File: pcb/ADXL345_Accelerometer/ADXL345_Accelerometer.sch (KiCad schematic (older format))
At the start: 16 parts, among them J1 Conn_01x09, Q1 BSS138, Q2 BSS138, U1 ADXL345_Library, U2 AP2112K-3.3

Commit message: Correcciones
Se corrigieron segun las recomendaciones realizadas por el docente.
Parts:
- U1: value ADXL345_Library -> ADXL345
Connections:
- net +3V3: now also R2.2, U1.1 (VDDI/O); no longer R2.1, U1.3 (RES)
- net GND: now also U1.2 (GND); no longer U1.1 (VDDI/O)
- net SCL: now also Q2.2 (S), R5.1; no longer Q2.3 (D), R5.2
- net VIN: now also R5.2; no longer R5.1
- net SDO: now reaches U1.12 (SDO)
- net SDO: now also J1.7 (Pin_7), R6.1
- net at U1.13 (SDA/SDI): now also Q1.2 (S), R1.2
- removed net SCL_3V: Q2.2 (S), R2.2, U1.14 (SCL/SCK)
- net SDA\SDIO renamed SDA
- removed net SDA\SDIO_3V: Q1.2 (S), R1.2, U1.10 (NC)
- removed net SDO\ADDR: J1.7 (Pin_7), R6.1, U1.11 (RES)
- new net: Q2.3 (D), R2.1, U1.14 (SCL/SCK)
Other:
- moved on the sheet: C1, C2, D1, H1, H2, J1, Q1, Q2, R1, R2, R3, R4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

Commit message: Correcciones
Se corrigieron detalles y se agregaron códigos de catálogo recomendados.
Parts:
- J1: Digi-Key (none) -> 10129378-909003BLF-ND; Link (none) -> https://ar.mouser.com/ProductDetail/Amphenol-FCI/10129378-9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; Manufacturer (none) -> Amphenol FCI; Supplier (none) -> Mouser
- Q1, Q2: Digi-Key (none) -> BSS138CT-ND; Link (none) -> https://www.digikey.com/product-detail/en/on-semiconductor/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; Manufacturer (none) -> Semiconductor Components Industries, LLC; Supplier (none) -> Digikey
- U1: Digi-Key (none) -> ADXL345BCCZ-ND; Link (none) -> https://www.digikey.com/product-detail/en/analog-devices-in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; Manufacturer (none) -> Analog Devices, Inc.; Supplier (none) -> Digikey
- U2: Digi-Key (none) -> AP2112K-3.3TRG1DITR-ND; Link (none) -> https://www.digikey.com/product-detail/en/diodes-incorporat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; Manufacturer (none) -> Diodes Incorporated; Supplier (none) -> Digikey
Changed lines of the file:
@@
 F 1 "ADXL345" V 6053 4224 50  0000 C CNN
 F 2 "Package_LGA:LGA-14_3x5mm_P0.8mm_LayoutBorder1x6y" H 6200 4125 50  0001 C CNN
-F 3 "" H 6200 4125 50  0001 C CNN
+F 3 "https://www.analog.com/media/en/technical-documentation/data-sheets/ADXL345.pdf" H 6200 4125 50  0001 C CNN
+F 4 "Analog Devices, Inc." V 6200 3550 50  0001 C CNN "Manufacturer"
+F 5 "https://ar.mouser.com/ProductDetail/Analog-Devices/ADXL345BCCZ?qs=WIvQP4zGanhoa7YOkGtvEg%3D%3D" V 6200 3550 50  0001 C CNN "Link"
+F 6 "Mouser" V 6200 3550 50  0001 C CNN "Supplier"
+F 7 "https://www.digikey.com/product-detail/en/analog-devices-inc/ADXL345BCCZ/ADXL345BCCZ-ND/2034829" V 6200 3550 50  0001 C CNN "Link"
+F 8 "Digikey" V 6200 3550 50  0001 C CNN "Supplier"
+F 9 "ADXL345BCCZ-ND" V 6200 3550 50  0001 C CNN "Digi-Key"
 	1    6200 3550
 	0    1    1    0
@@
 F 2 "Package_TO_SOT_SMD:SOT-23-5" H 5300 1975 50  0001 C CNN
 F 3 "https://www.diodes.com/assets/Datasheets/AP2112.pdf" H 5300 1750 50  0001 C CNN
+F 4 "Diodes Incorporated" H 5300 1650 50  0001 C CNN "Manufacturer"
+F 5 "https://ar.mouser.com/ProductDetail/Diodes-Incorporated/AP2112K-33TRG1?qs=x6A8l6qLYDDPYHosCdzh%2FA%3D%3D" H 5300 1650 50  0001 C CNN "Link"
+F 6 "Mouser" H 5300 1650 50  0001 C CNN "Supplier"
+F 7 "https://www.digikey.com/product-detail/en/diodes-incorporated/AP2112K-3-3TRG1/AP2112K-3-3TRG1DITR-ND/4470746" H 5300 1650 50  0001 C CNN "Link"
+F 8 "Digikey" H 5300 1650 50  0001 C CNN "Supplier"
+F 9 "AP2112K-3.3TRG1DITR-ND" H 5300 1650 50  0001 C CNN "Digi-Key"
 	1    5300 1650
 	1    0    0    -1
@@
 F 1 "Conn_01x09" V 3800 3300 50  0000 L CNN
 F 2 "Connector_PinHeader_2.54mm:PinHeader_1x09_P2.54mm_Vertical" H 3650 3650 50  0001 C CNN
-F 3 "~" H 3650 3650 50  0001 C CNN
+F 3 "https://www.amphenol-icc.com/media/wysiwyg/files/documentation/datasheet/boardwiretoboard/bwb_bergstik.pdf" H 3650 3650 50  0001 C CNN
+F 4 "Amphenol FCI" V 3650 3650 50  0001 C CNN "Manufacturer"
+F 5 "https://ar.mouser.com/ProductDetail/Amphenol-FCI/10129378-909003BLF?qs=0lQeLiL1qyYKryXpJ%252BfC%252BQ%3D%3D" V 3650 3650 50  0001 C CNN "Link"
+F 6 "Mouser" V 3650 3650 50  0001 C CNN "Supplier"
+F 7 "10129378-909003BLF-ND" V 3650 3650 50  0001 C CNN "Digi-Key"
 	1    3650 3650
 	-1   0    0    -1
@@
 F 1 "BSS138" V 5700 5800 50  0000 C CNN
 F 2 "Package_TO_SOT_SMD:SOT-23" H 5550 5725 50  0001 L CIN
-F 3 "https://www.fairchildsemi.com/datasheets/BS/BSS138.pdf" H 5350 5800 50  0001 L CNN
+F 3 "https://www.onsemi.com/pub/Collateral/BSS138-D.PDF" H 5350 5800 50  0001 L CNN
+F 4 "Semiconductor Components Industries, LLC " V 5350 5800 50  0001 C CNN "Manufacturer"
+F 5 "https://ar.mouser.com/ProductDetail/ON-Semiconductor-Fairchild/BSS138?qs=HK%252BeIG1iaahCeqBvjB4arg%3D%3D" V 5350 5800 50  0001 C CNN "Link"
+F 6 "Mouser" V 5350 5800 50  0001 C CNN "Supplier"
+F 7 "https://www.digikey.com/product-detail/en/on-semiconductor/BSS138/BSS138CT-ND/244294" V 5350 5800 50  0001 C CNN "Link"
+F 8 "Digikey" V 5350 5800 50  0001 C CNN "Supplier"
+F 9 "BSS138CT-ND" V 5350 5800 50  0001 C CNN "Digi-Key"
 	1    5350 5800
 	0    1    1    0
@@
 F 1 "BSS138" V 6000 4900 50  0000 C CNN
 F 2 "Package_TO_SOT_SMD:SOT-23" H 5950 4825 50  0001 L CIN
-F 3 "https://www.fairchildsemi.com/datasheets/BS/BSS138.pdf" H 5750 4900 50  0001 L CNN
+F 3 "https://www.onsemi.com/pub/Collateral/BSS138-D.PDF" H 5750 4900 50  0001 L CNN
+F 4 "Semiconductor Components Industries, LLC " V 5750 4900 50  0001 C CNN "Manufacturer"
+F 5 "https://ar.mouser.com/ProductDetail/ON-Semiconductor-Fairchild/BSS138?qs=HK%252BeIG1iaahCeqBvjB4arg%3D%3D" V 5750 4900 50  0001 C CNN "Link"
+F 6 "Mouser" V 5750 4900 50  0001 C CNN "Supplier"
+F 7 "https://www.digikey.com/product-detail/en/on-semiconductor/BSS138/BSS138CT-ND/244294" V 5750 4900 50  0001 C CNN "Link"
+F 8 "Digikey" V 5750 4900 50  0001 C CNN "Supplier"
+F 9 " BSS138CT-ND" V 5750 4900 50  0001 C CNN "Digi-Key"
 	1    5750 4900
 	0    -1   -1   0

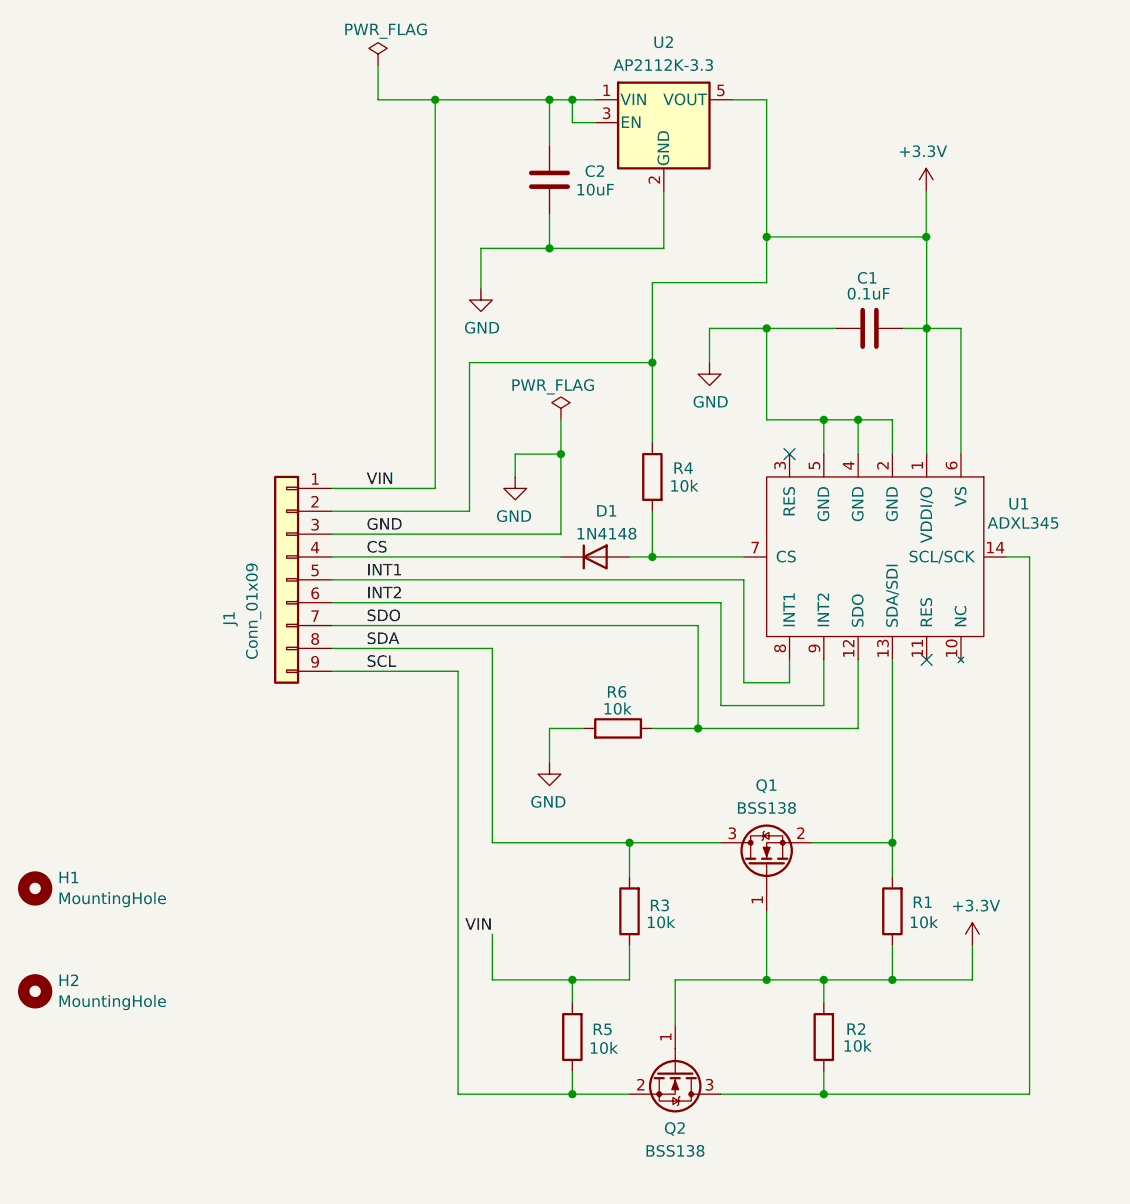
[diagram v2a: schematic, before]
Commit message: Se agregaron fiduciales
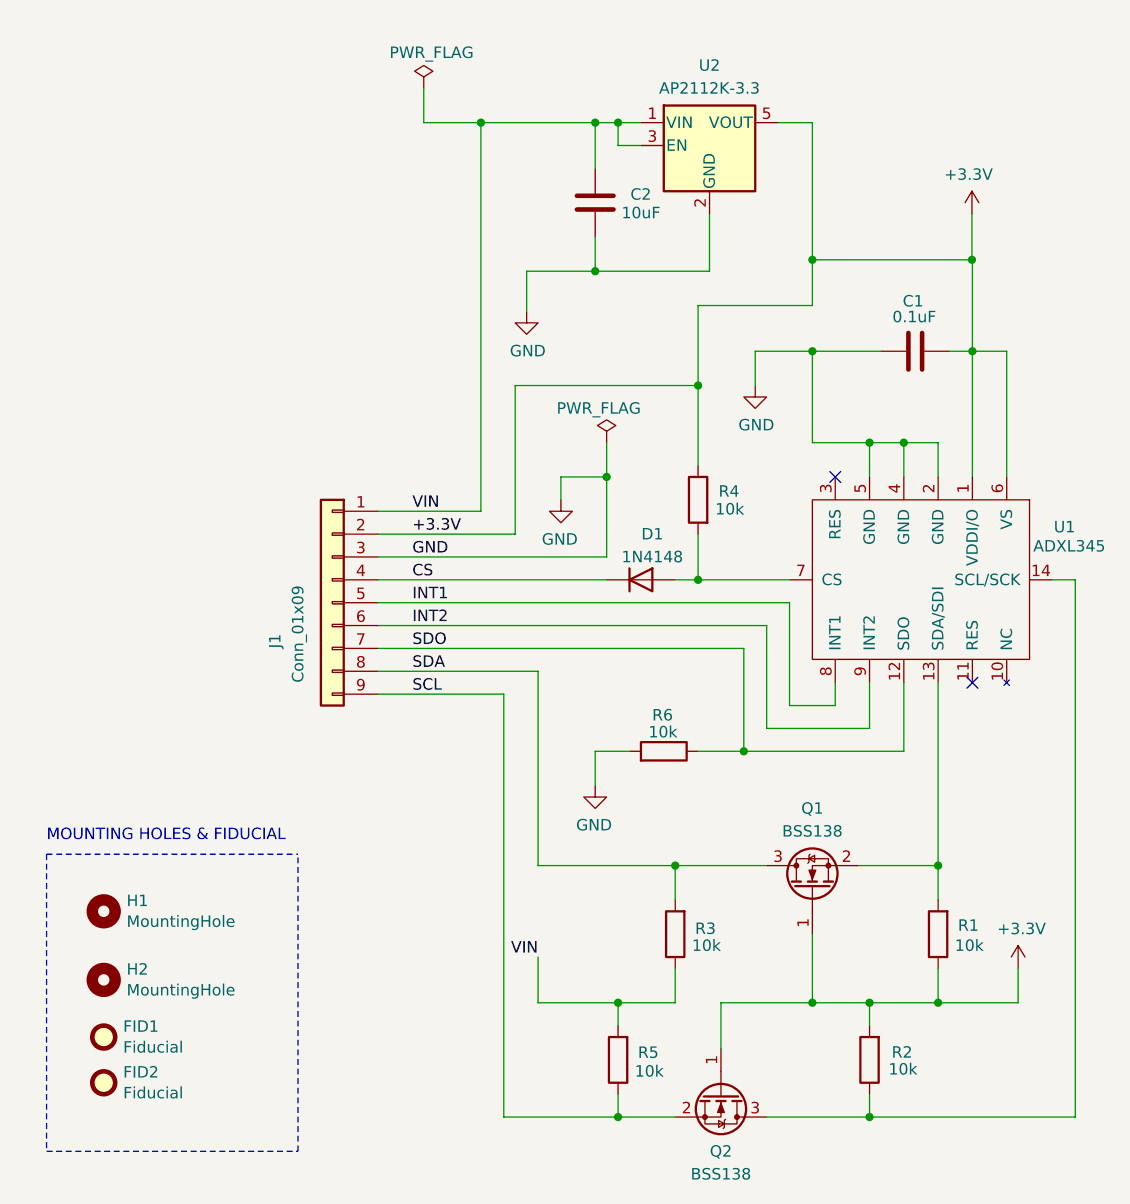
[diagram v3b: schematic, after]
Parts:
- added FID1, FID2: Fiducial, Fiducial:Fiducial_0.5mm_Mask1.5mm, symbol Mechanical:Fiducial
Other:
- note added: "MOUNTING HOLES & FIDUCIAL"
- moved on the sheet: C1, C2, D1, H1, H2, J1, Q1, Q2, R1, R2, R3, R4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

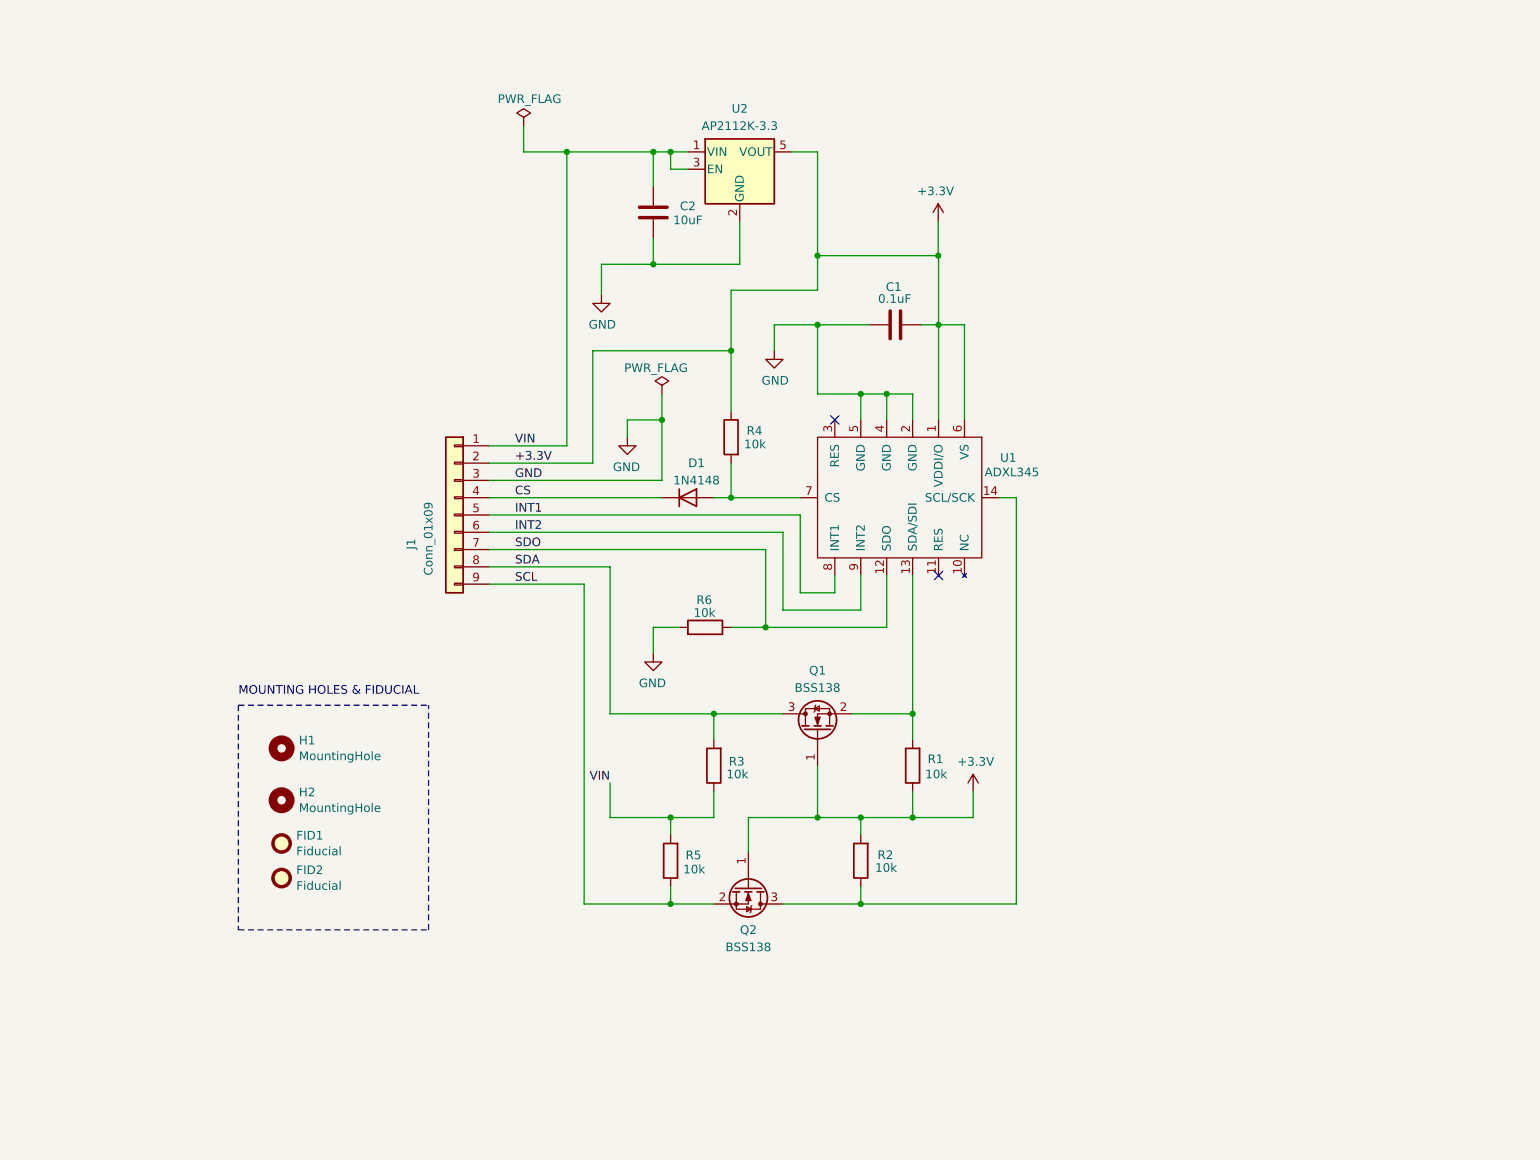
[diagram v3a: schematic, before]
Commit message: Correcciones
Se hicieron las correcciones de acuerdo a las recomendaciones del docente.
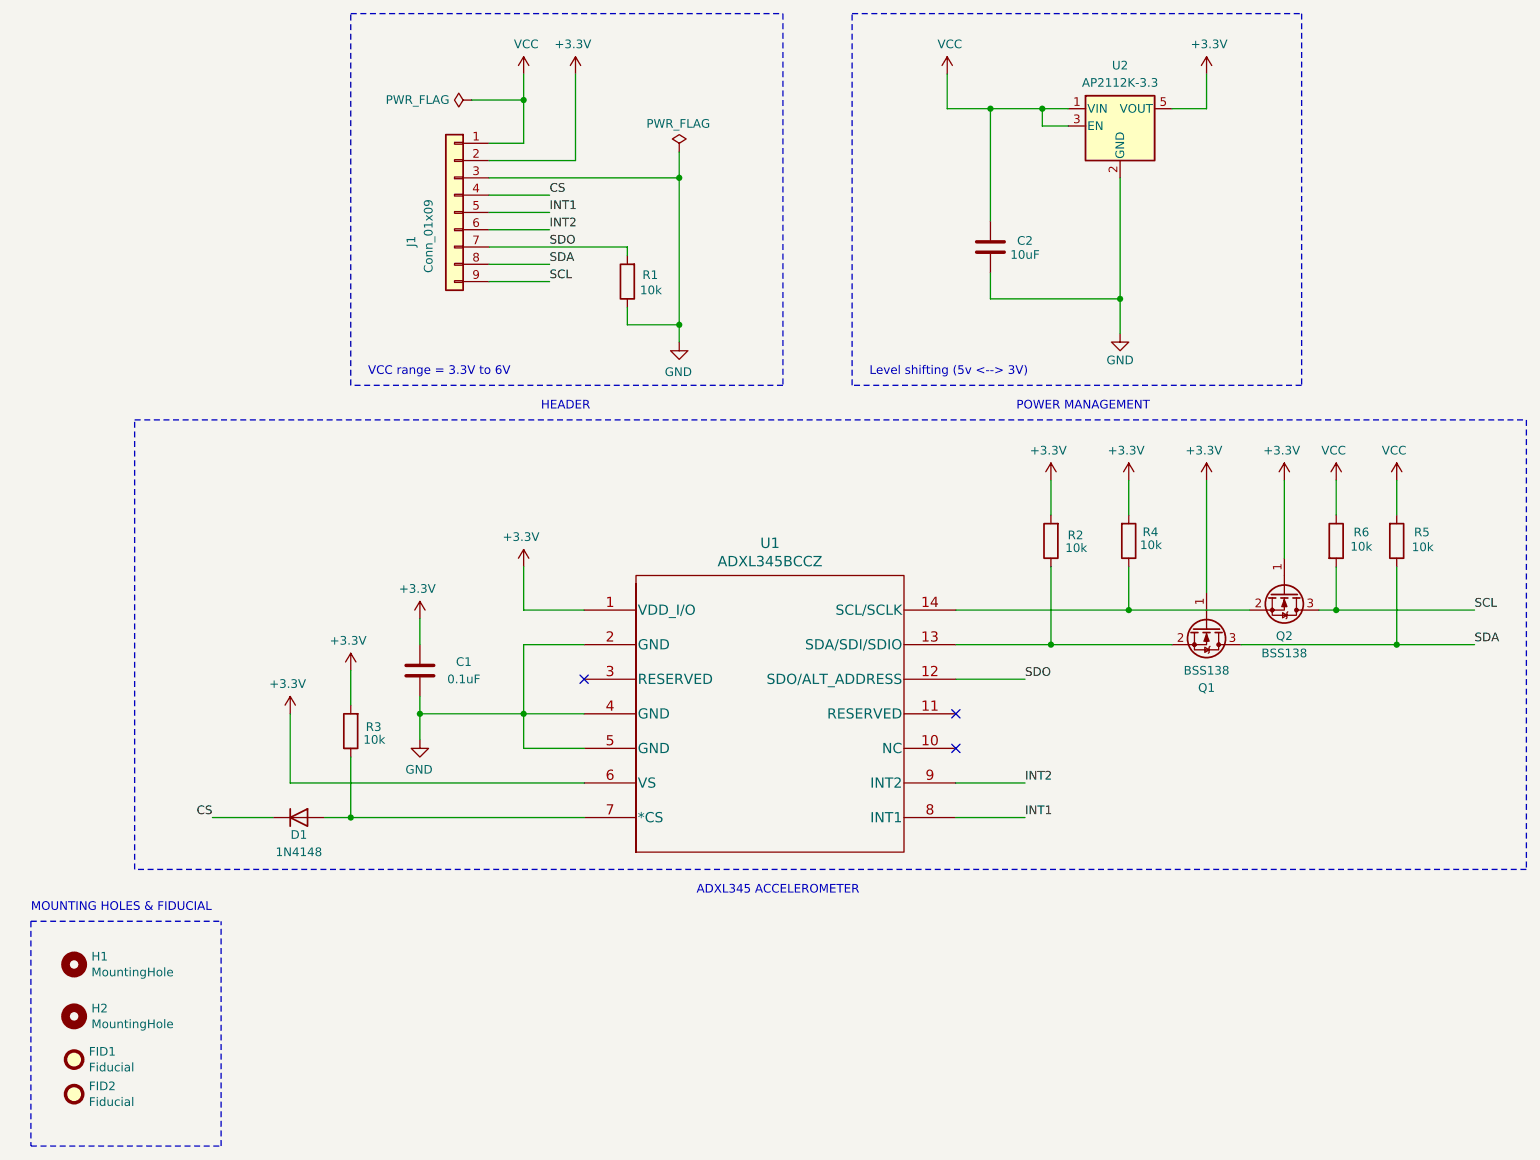
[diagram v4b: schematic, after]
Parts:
- removed U1: ADXL345, Package_LGA:LGA-14_3x5mm_P0.8mm_LayoutBorder1x6y, symbol ADXL345:ADXL345_Library
- added U1: ADXL345BCCZ, Package_LGA:LGA-14_3x5mm_P0.8mm_LayoutBorder1x6y, symbol ADXL345BCCZ:ADXL345BCCZ
- R1, R2, R3, R4, R5, R6: footprint Resistor_SMD:R_0603_1608Metric -> Diode_SMD:D_0805_2012Metric
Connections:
- net +3V3: now also C1.2, R3.2, R4.2, U1.1 (VDD_I/O), U1.6 (VS); no longer C1.1, R1.1, R4.1
- net GND: now also C1.1, R1.1, U1.2 (GND), U1.4 (GND), U1.5 (GND); no longer C1.2, R6.2
- net INT1: now also U1.8 (INT1)
- net INT2: now also U1.9 (INT2)
- net SCL: now also Q2.3 (D), R6.2; no longer Q2.2 (S), R5.1
- net SDA: now also R5.1; no longer R3.2
- net SDO: now also R1.2, U1.12 (SDO/ALT_ADDRESS); no longer R6.1
- net at D1.2 (A): now also R3.1, U1.7 (*CS); no longer R4.2
- net at Q1.2 (S): now also R2.1, U1.13 (SDA/SDI/SDIO); no longer R1.2
- net VIN renamed VCC
- net VCC: now also R6.1; no longer R3.1
- new net: Q2.2 (S), R4.1, U1.14 (SCL/SCLK)
- no-connect marks 2 -> 3
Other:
- note added: "ADXL345 ACCELEROMETER"
- note added: "HEADER"
- note added: "Level shifting (5v <--> 3V)"
- note added: "POWER MANAGEMENT"
- note added: "VCC range = 3.3V to 6V"
- moved on the sheet: C1, C2, D1, FID1, FID2, H1, H2, J1, Q1, Q2, R1, R2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

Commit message: Modelos 3D
Se generaron los modelos 3D.
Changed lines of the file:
@@
 	1    0    0    -1
 $EndComp
-Text Notes 1400 6050 0    50   ~ 0
+Text Notes 1300 6050 0    58   ~ 12
 MOUNTING HOLES & FIDUCIAL
 Wire Notes Line
@@
 	1    0    0    -1
 $EndComp
-Text Notes 5250 5950 0    50   ~ 0
+Text Notes 5500 5950 0    58   ~ 12
 ADXL345 ACCELEROMETER
 Text Notes 6250 2950 0    50   ~ 0
@@
 	1    0    0    -1
 $EndComp
-Text Notes 4350 3150 0    50   ~ 0
-HEADER
 Wire Notes Line
 	3250 850  5750 850
@@
 Wire Notes Line
 	8750 3000 6150 3000
-Text Notes 7100 3150 0    50   ~ 0
+Text Notes 7100 3150 0    58   ~ 12
 POWER MANAGEMENT
 $Comp
@@
 Wire Wire Line
 	9300 4500 9750 4500
+Text Notes 4350 3150 0    58   ~ 12
+HEADER
 $EndSCHEMATC
